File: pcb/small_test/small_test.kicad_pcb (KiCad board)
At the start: 2 copper layers, 76.2 x 50.8 mm, 5 parts, among them U1 ArduinoNano_r3.3

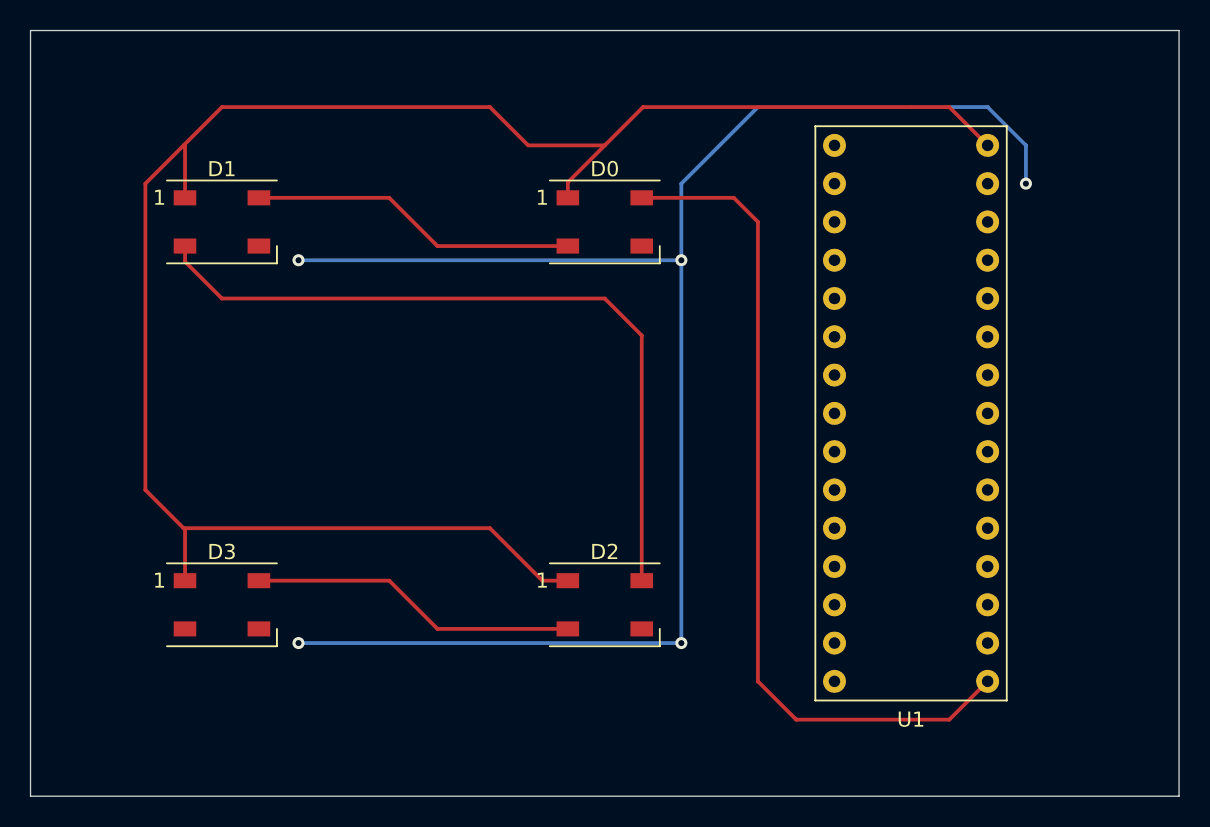
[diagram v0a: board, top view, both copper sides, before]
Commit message: Update test PCB with new symbols and added caps
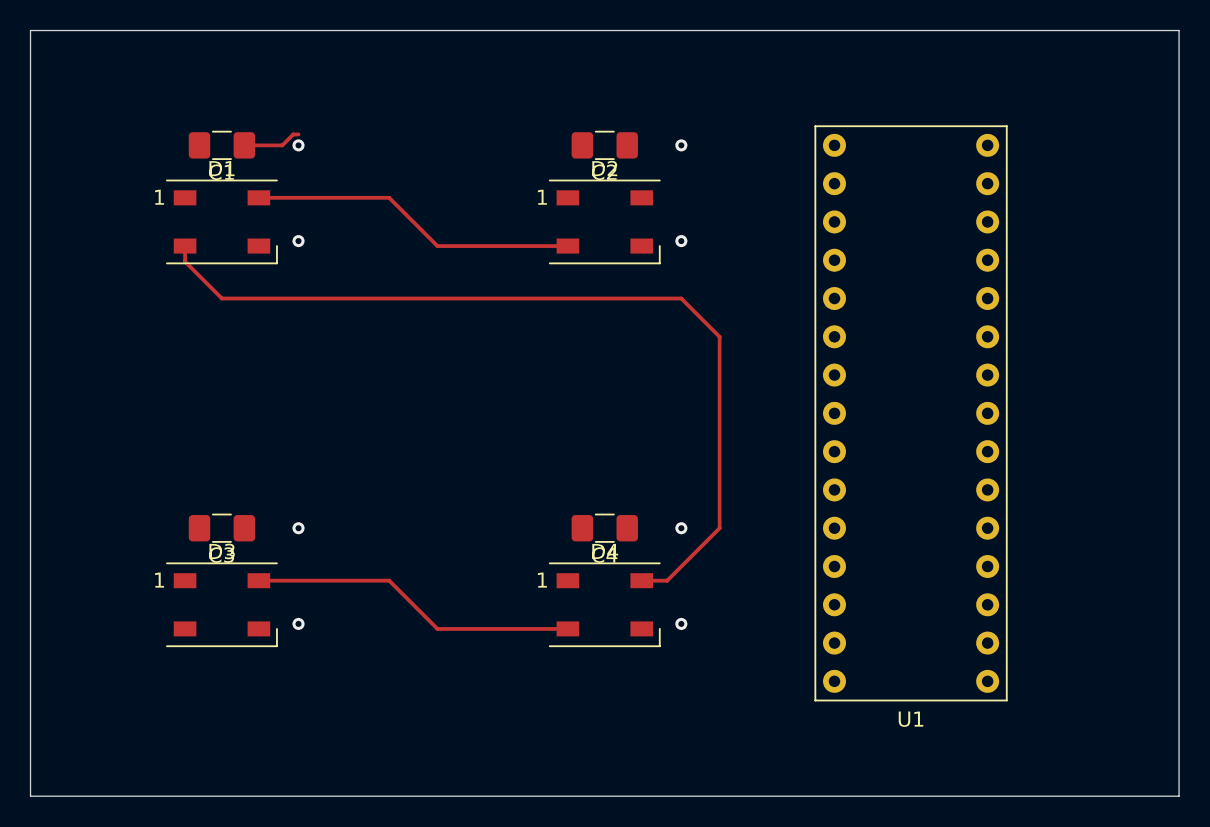
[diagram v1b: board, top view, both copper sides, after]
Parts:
- removed D0: WS2812B, LED_SMD:LED_WS2812B_PLCC4_5.0x5.0mm_P3.2mm
- added C1: C, Capacitor_SMD:C_1206_3216Metric_Pad1.42x1.75mm_HandSolder, F.Cu at (63.5, 58.4)
- added C2: C, Capacitor_SMD:C_1206_3216Metric_Pad1.42x1.75mm_HandSolder, F.Cu at (88.9, 58.4)
- added C3: C, Capacitor_SMD:C_1206_3216Metric_Pad1.42x1.75mm_HandSolder, F.Cu at (63.5, 83.8)
- added C4: C, Capacitor_SMD:C_1206_3216Metric_Pad1.42x1.75mm_HandSolder, F.Cu at (88.9, 83.8)
- added D4: Neopixel5050, LED_SMD:LED_WS2812B_PLCC4_5.0x5.0mm_P3.2mm, F.Cu at (88.9, 88.9)
- D1, D2, D3: value WS2812B -> Neopixel5050
- moved D2 25.4 mm to (88.9, 63.5)
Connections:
- net G_GND renamed GND
- D1 pad 2: Net-(D1-Pad2) -> LED_R0t1
- D1 pad 4: Net-(D0-Pad2) -> Net-(D1-Pad4)
- D2 pad 2: Net-(D2-Pad2) -> Net-(D1-Pad4)
- D2 pad 4: Net-(D1-Pad2) -> LED_DATA
- D3 pad 4: Net-(D2-Pad2) -> Net-(D3-Pad4)
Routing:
- net G_VCC: track 123.5 -> 0.00 mm
- net (no net): track 109.8 -> 0.00 mm, vias 5 -> 8
- net LED_R0t1: track 0.00 -> 57.9 mm
- net LED_DATA: track 56.2 -> 0.00 mm
- net Net-(D1-Pad2): track 49.6 -> 0.00 mm
- net Net-(D3-Pad4): track 0.00 -> 21.8 mm
- net Net-(D2-Pad2): track 21.8 -> 0.00 mm
- net Net-(D1-Pad4): track 0.00 -> 21.8 mm
- net Net-(D0-Pad2): track 21.8 -> 0.00 mm
- net GND: track 0.00 -> 3.89 mm

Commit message: Update test PCB
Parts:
- added REF**: MountingHole_3.2mm_M3, MountingHole:MountingHole_3.2mm_M3, F.Cu at (123.2, 97.8)
- added REF**: MountingHole_3.2mm_M3, MountingHole:MountingHole_3.2mm_M3, F.Cu at (54.6, 97.8)
- added REF**: MountingHole_3.2mm_M3, MountingHole:MountingHole_3.2mm_M3, F.Cu at (54.6, 54.6)
- added REF**: MountingHole_3.2mm_M3, MountingHole:MountingHole_3.2mm_M3, F.Cu at (123.2, 54.6)
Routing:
- net G_VCC: track 0.00 -> 149.4 mm
- net LED_DATA: track 0.00 -> 55.5 mm
- net GND: track 3.89 -> 25.4 mm, vias 0 -> 8
- net (no net): vias 8 -> 0
- added copper zone on B.Cu, net GND
